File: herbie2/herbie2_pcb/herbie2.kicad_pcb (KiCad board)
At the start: 2 copper layers, 119.4 x 96.5 mm, 90 parts, among them J1 GND, J10 CONN_04JST-PTH, J11 CONN_04JST-PTH, J12 Vin, J15 Conn_01x03_Male, J16 Conn_02x03_Odd_Even, J17 Conn_01x03, J18 Conn_01x02, J19 Conn_01x01, J2 5V, J20 Conn_01x03, J3 I2C_STANDARDQWIIC, J4 Conn_01x01, J5 Conn_01x02, J8 I2C_STANDARDQWIIC, J9 I2C_STANDARDQWIIC, Q1 LTC4412, Q2 LTC4412, Q3 Si4427, Q4 Si4427, Q5 2N7002, U1 74HC595, U2 74164, U3 24v13_Pololu, U4 LS7366R, U5 LS7366R, U6 TCA9534, U7 24v13_Pololu, U8 D36V50F5_Pololu, Y1 20MHz, Y2 20MHz

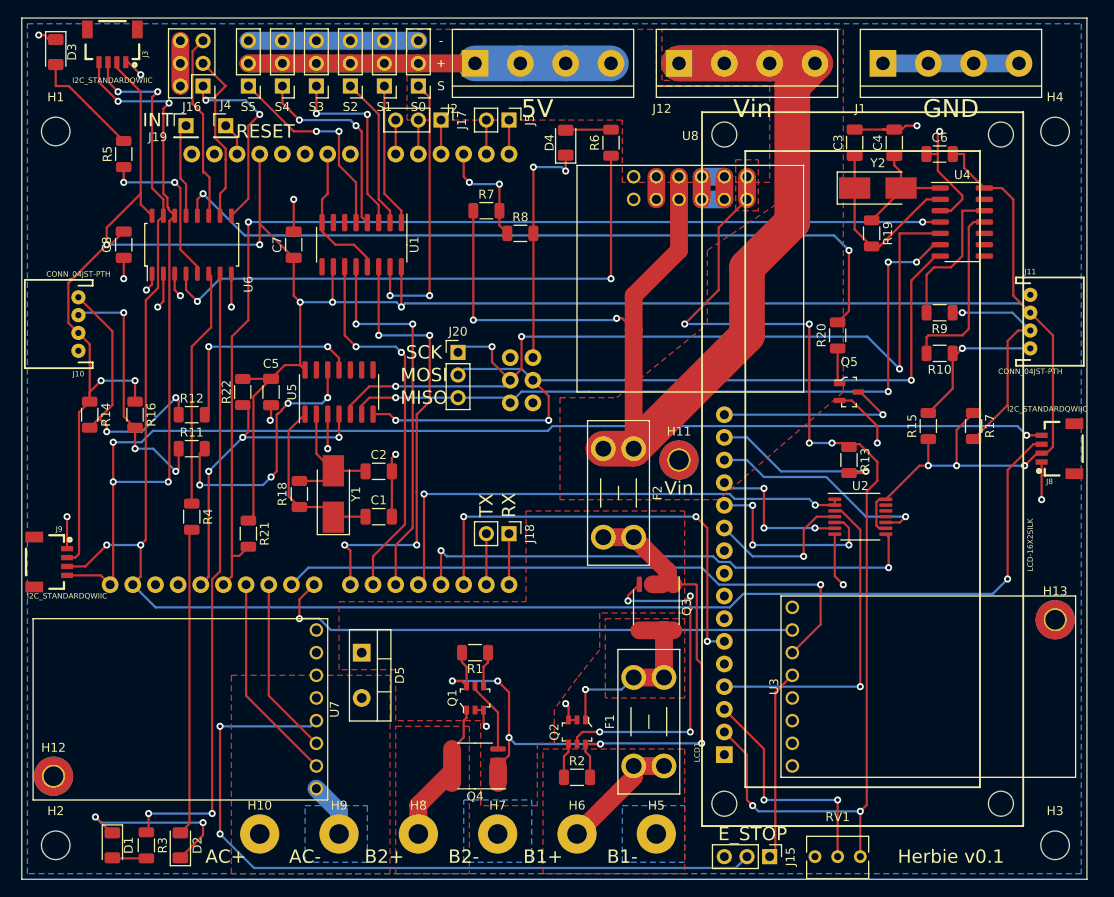
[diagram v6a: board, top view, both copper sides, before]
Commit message: changed PWM pins
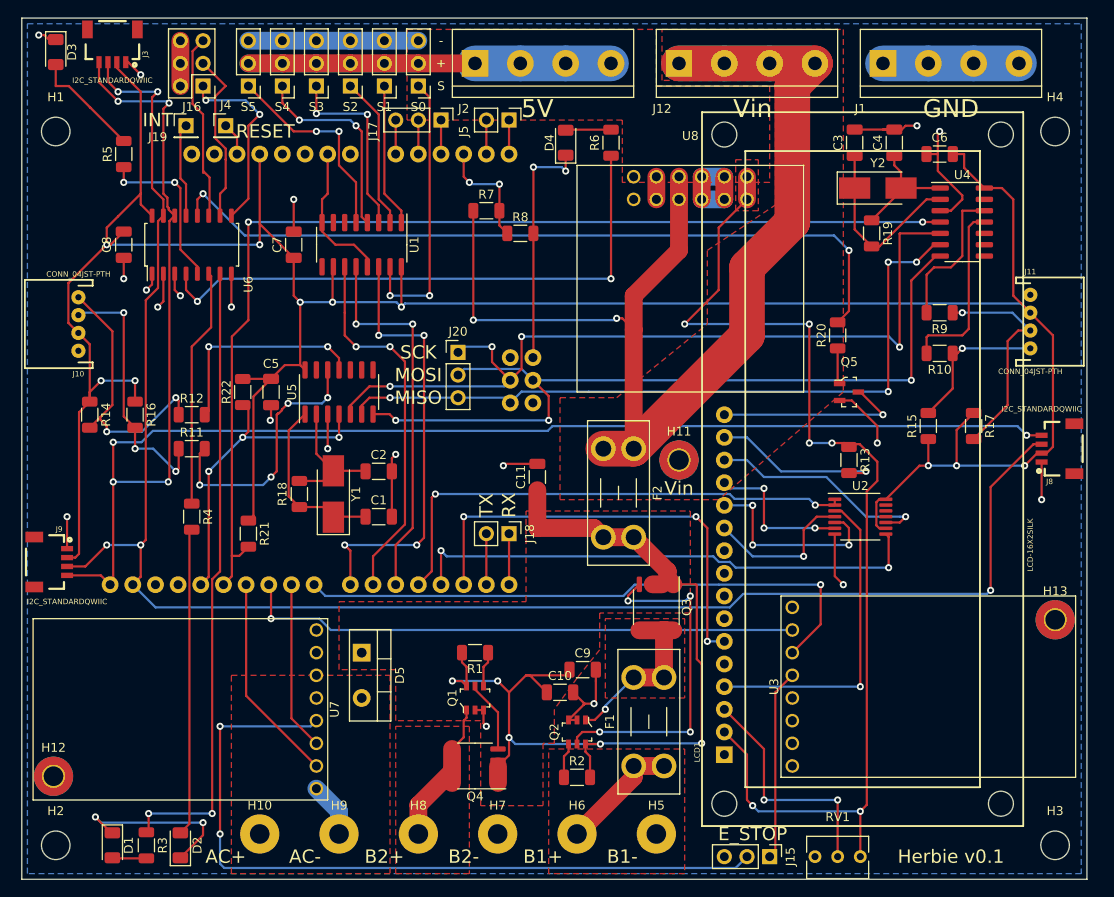
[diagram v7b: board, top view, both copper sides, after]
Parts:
- added C10: 1uF, Capacitor_SMD:C_1206_3216Metric, F.Cu at (163.2, 114.9)
- added C11: 10uF, Capacitor_SMD:C_1206_3216Metric, F.Cu at (160.7, 90.8)
- added C9: .1uF, Capacitor_SMD:C_1206_3216Metric, F.Cu at (165.7, 112.4)
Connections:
- B2 pad D10: MOTOR2_PWM -> MOTOR1_DIR
- B2 pad D8: MOTOR1_DIR -> MOTOR1_PWM
- B2 pad D9: MOTOR1_PWM -> MOTOR2_PWM
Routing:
- net VIN_FUSE: track 83.5 -> 105.6 mm
- net GND: track 203.0 -> 214.3 mm, vias 23 -> 24
- net ENC_SCK: track 98.4 -> 95.0 mm
- net MOTOR1_DIR: track 60.3 -> 63.4 mm
- net MOTOR1_PWM: track 69.8 -> 66.8 mm
- net E_STOP2: track 84.3 -> 86.2 mm
- net BATT1_F: track 21.8 -> 20.1 mm
- net MOTOR2_PWM: track 20.5 -> 18.9 mm
- net DATA_SERVO: track 50.3 -> 49.4 mm
- net DATA_LCD: track 57.6 -> 56.9 mm

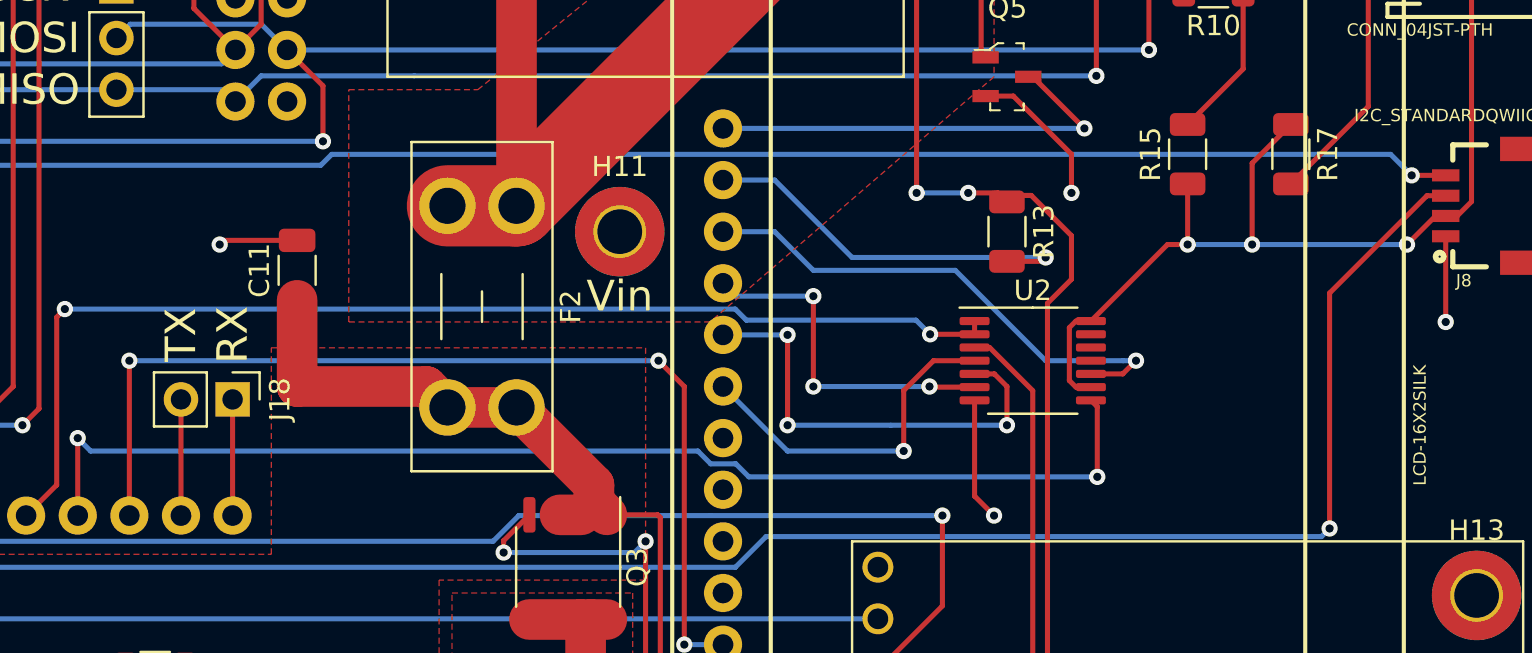
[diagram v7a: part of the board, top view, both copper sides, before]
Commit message: added i2c pullup resistors
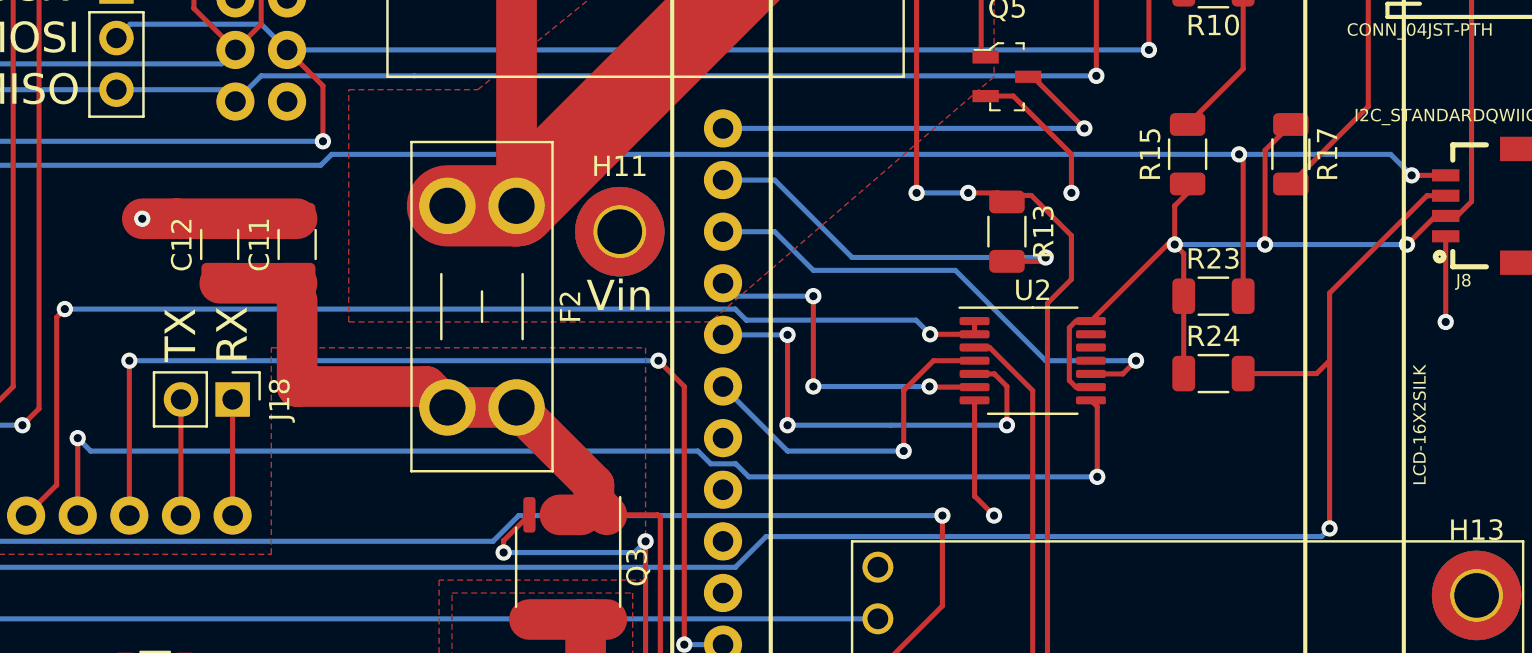
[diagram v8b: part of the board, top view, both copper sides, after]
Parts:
- added C12: 10uF, Capacitor_SMD:C_1206_3216Metric, F.Cu at (156.8, 89.5)
- added R23: R, Resistor_SMD:R_1206_3216Metric, F.Cu at (205.7, 92.1)
- added R24: R, Resistor_SMD:R_1206_3216Metric, F.Cu at (205.7, 95.9)
- moved C11 1.27 mm to (160.7, 89.5)
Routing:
- net SCL: track 187.4 -> 194.2 mm, vias 6 -> 7
- net 3.3V: track 312.6 -> 319.2 mm
- net SDA: track 192.2 -> 196.7 mm
- net VIN_FUSE: track 105.6 -> 109.5 mm
- net GND: track 214.3 -> 218.0 mm
